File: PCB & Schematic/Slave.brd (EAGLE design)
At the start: 62.2 x 48.3 mm, 55 parts, among them J1 CH1, J10 CH10, J11 GND, J2 CH2, J3 CH3, J4 CH4, J5 CH5, J6 CH6, J7 CH7, J8 CH8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

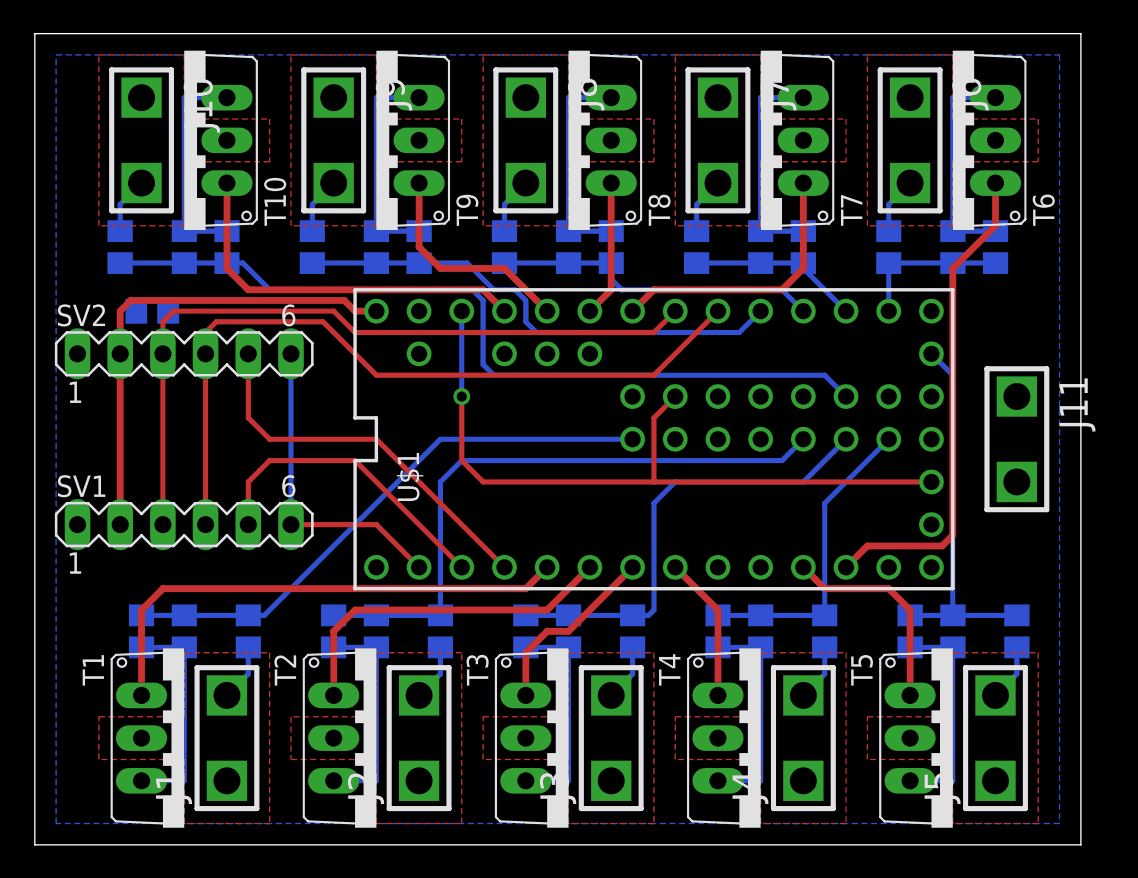
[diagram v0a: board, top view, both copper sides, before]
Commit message: Update PCB layout.
Made component names legible, and added some text to indicate what
gets plugged in where.

This version was sent to OHS Park. Hopefully it works!
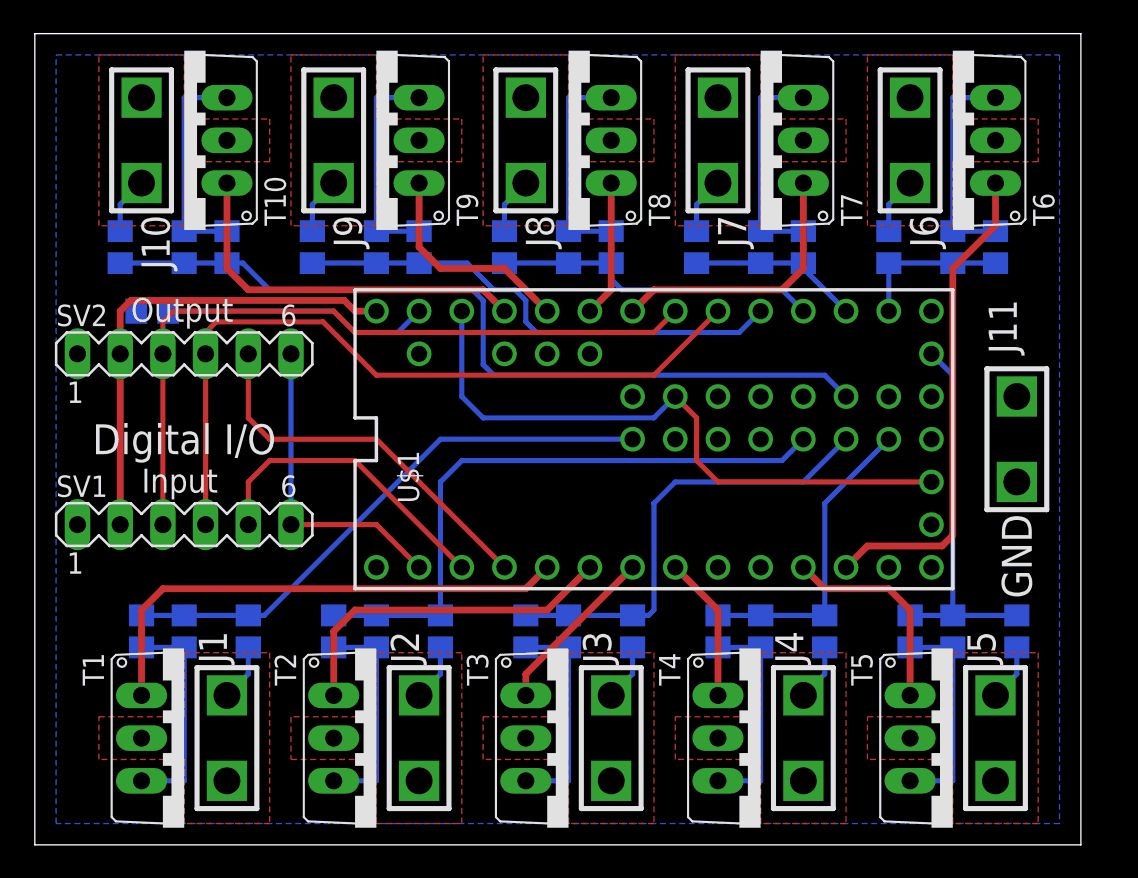
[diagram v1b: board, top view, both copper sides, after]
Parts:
- turned J11 to 90 degrees
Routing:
- net AGND: track 0.00 -> 16.0 mm
- net 3.3V: track 43.0 -> 37.7 mm, vias 1 -> 0
- net CHIME3: track 11.0 -> 10.3 mm
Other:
- board text added: "Digital I/O"
- board text added: "GND"
- board text added: "Input"
- board text added: "MIDI Chimes Slave Board DAVe3283 2016-01-03"
- board text added: "Output"
